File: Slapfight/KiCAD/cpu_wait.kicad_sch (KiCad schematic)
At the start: 6 parts, among them U1A_ 74LS74, U2A_ 74LS74, U2B_ 74LS32, U3A_ 74LS04, U4A_ 74LS08, U9A_ 74LS08

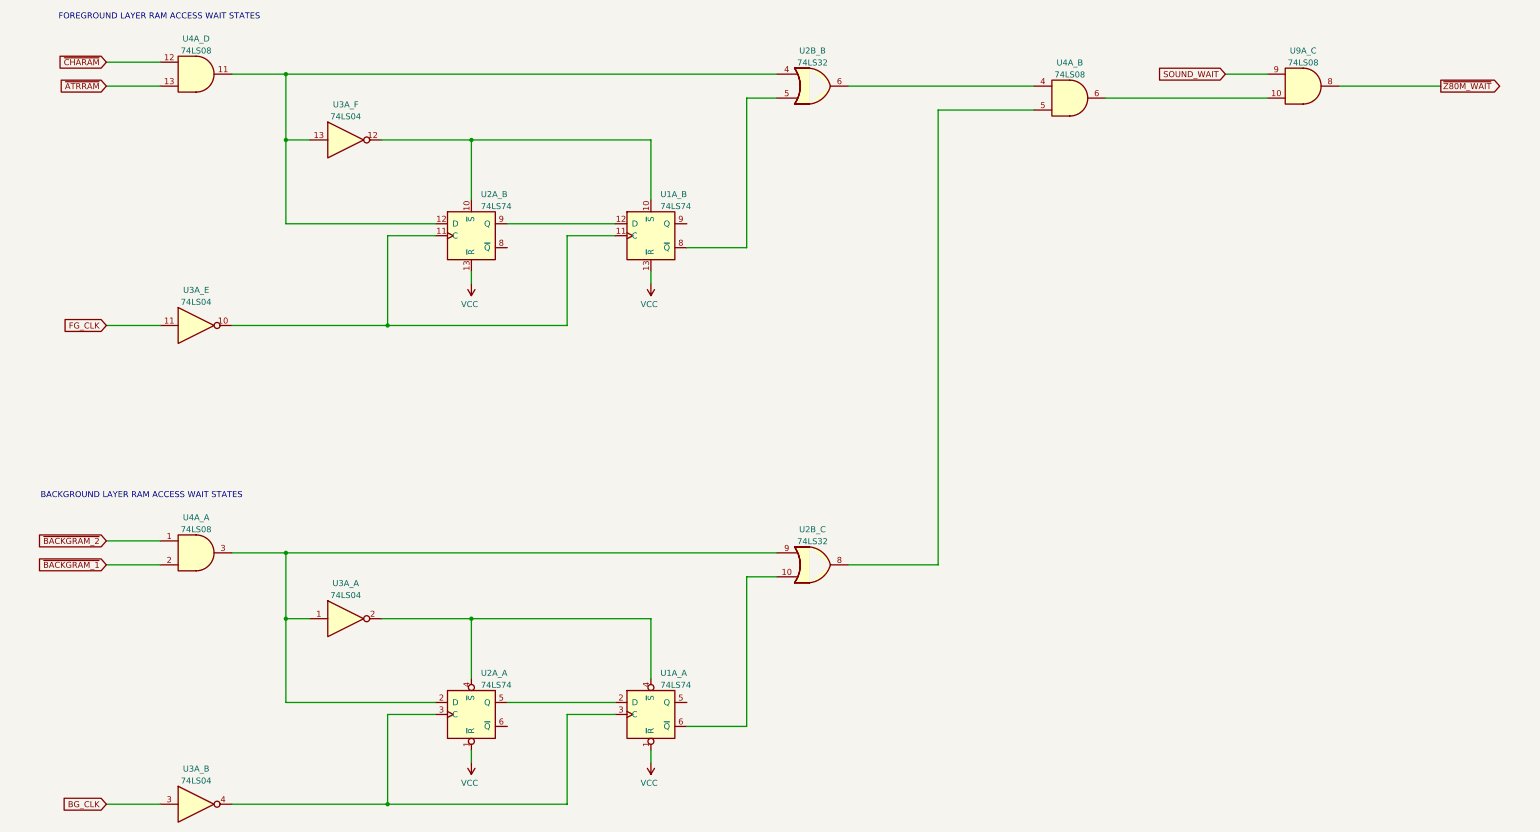
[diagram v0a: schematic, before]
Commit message: Component naming updates
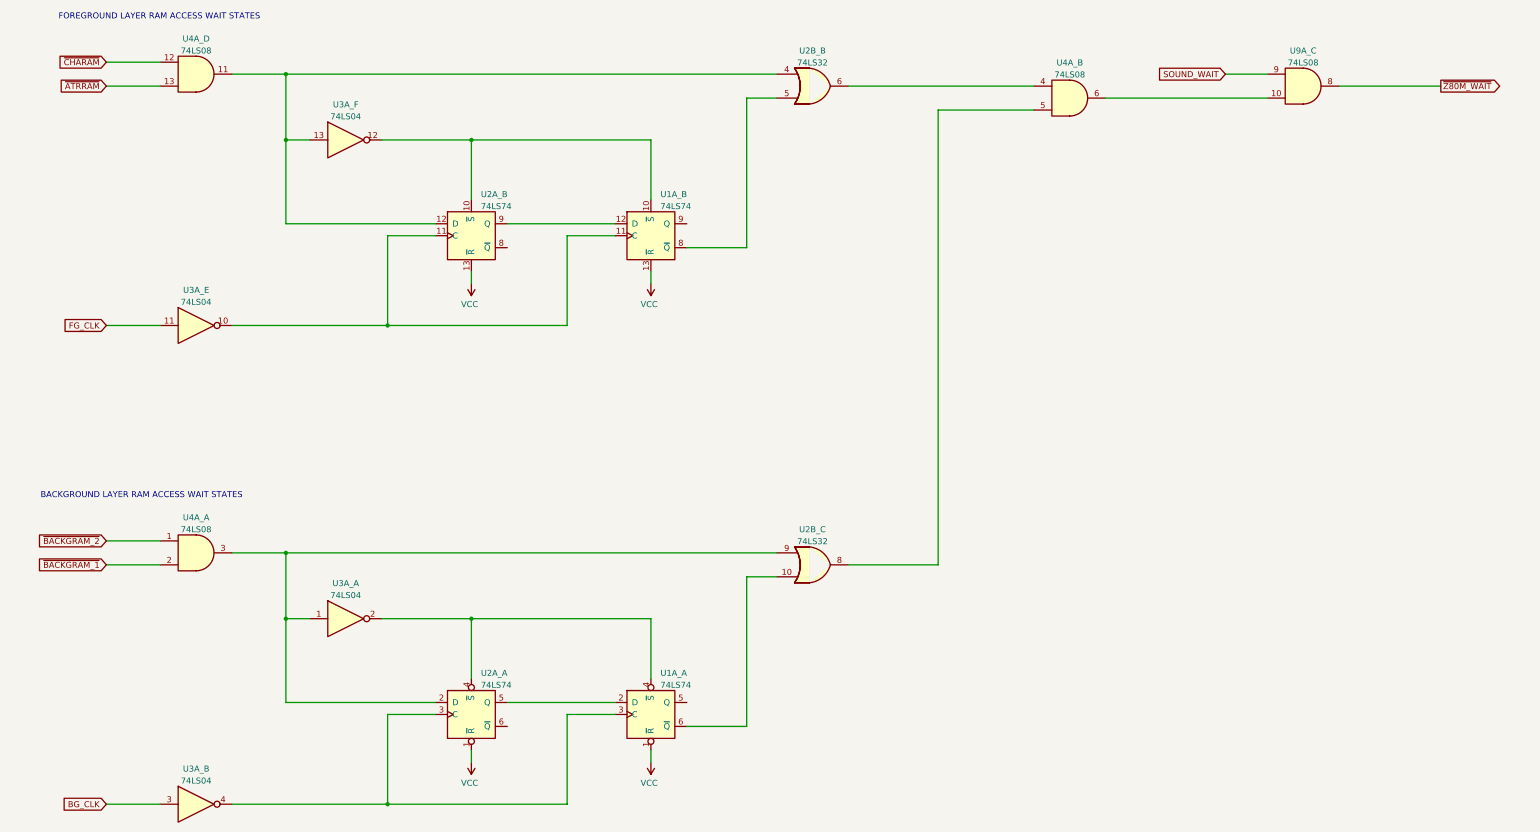
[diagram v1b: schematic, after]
